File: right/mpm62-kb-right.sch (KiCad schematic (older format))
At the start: 81 parts

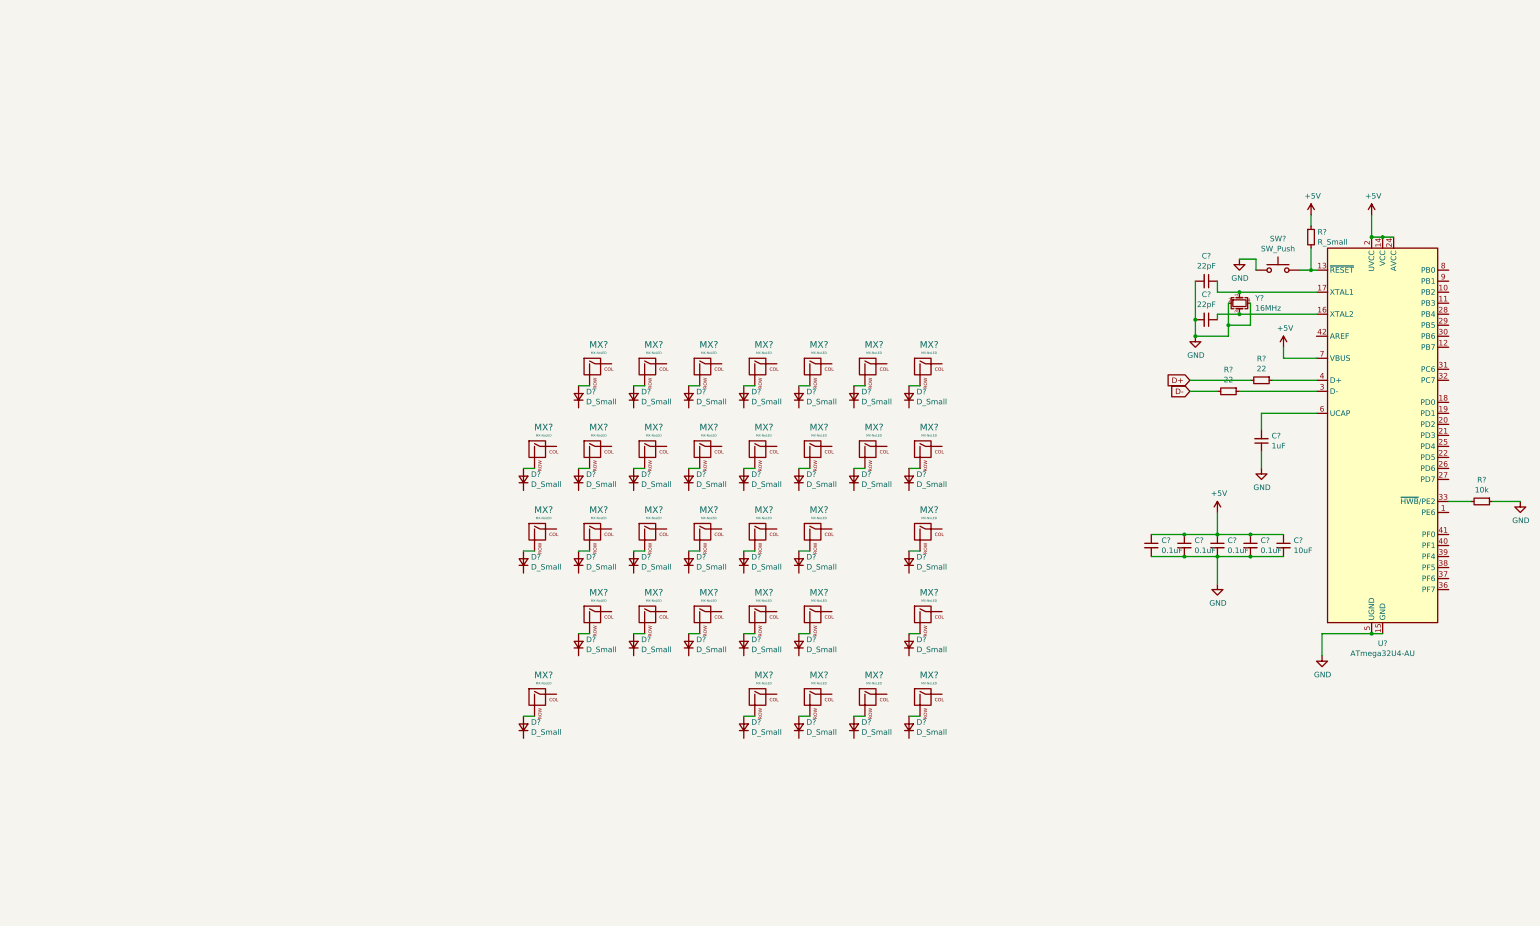
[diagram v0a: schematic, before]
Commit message: complete schematics for both left and right
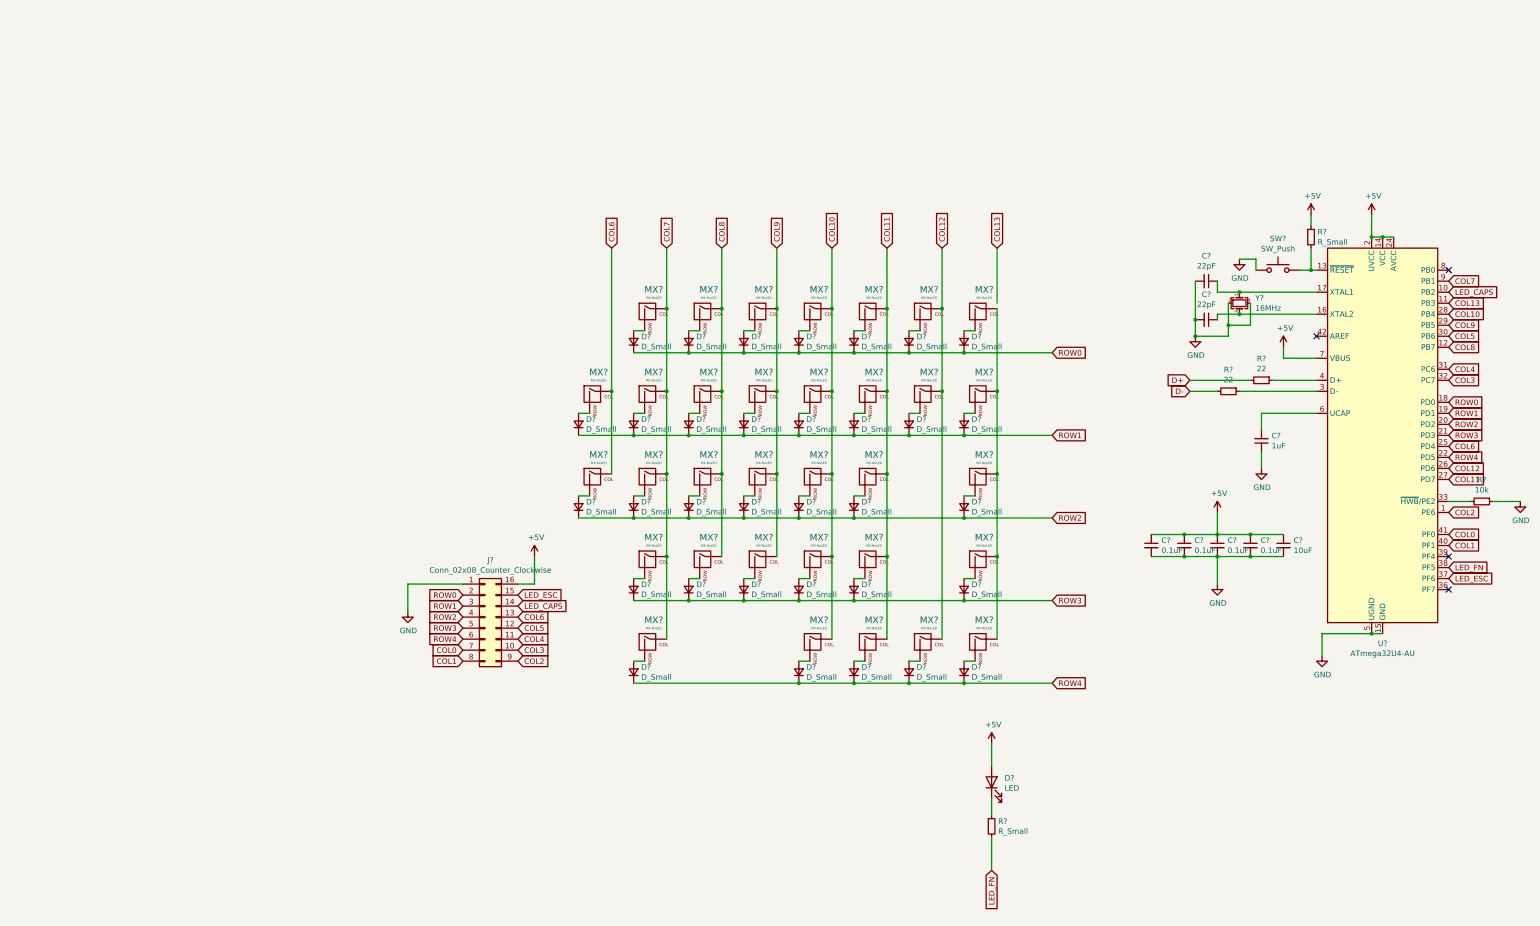
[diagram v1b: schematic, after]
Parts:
- added D?: LED, symbol Device:LED
- added J?: Conn_02x08_Counter_Clockwise, symbol Connector_Generic:Conn_02x08_Counter_Clockwise
- added R?: R_Small, symbol Device:R_Small
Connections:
- net +5V: now also D?.2 (A), J?.16 (Pin_16)
- net GND: now also J?.1 (Pin_1)
- net ROW1: now reaches D?.1 (K)
- net ROW1: now also D?.1 (K), D?.1 (K), D?.1 (K), D?.1 (K), D?.1 (K), D?.1 (K), D?.1 (K), U?.19 (PD1), J?.3 (Pin_3)
- net COL6: now reaches MX?.1 (COL)
- net COL6: now also MX?.1 (COL), U?.25 (PD4), J?.13 (Pin_13)
- net ROW2: now reaches D?.1 (K)
- net ROW2: now also D?.1 (K), D?.1 (K), D?.1 (K), D?.1 (K), D?.1 (K), D?.1 (K), U?.20 (PD2), J?.4 (Pin_4)
- net ROW4: now reaches D?.1 (K)
- net ROW4: now also D?.1 (K), D?.1 (K), D?.1 (K), D?.1 (K), U?.22 (PD5), J?.6 (Pin_6)
- net COL7: now reaches MX?.1 (COL)
- net COL7: now also MX?.1 (COL), MX?.1 (COL), MX?.1 (COL), MX?.1 (COL), U?.9 (PB1)
- net ROW0: now reaches D?.1 (K)
- net ROW0: now also D?.1 (K), D?.1 (K), D?.1 (K), D?.1 (K), D?.1 (K), D?.1 (K), U?.18 (PD0), J?.2 (Pin_2)
- net ROW3: now reaches D?.1 (K)
- net ROW3: now also D?.1 (K), D?.1 (K), D?.1 (K), D?.1 (K), D?.1 (K), U?.21 (PD3), J?.5 (Pin_5)
- net COL8: now reaches MX?.1 (COL)
- net COL8: now also MX?.1 (COL), MX?.1 (COL), MX?.1 (COL), U?.12 (PB7)
- net COL9: now reaches MX?.1 (COL)
- net COL9: now also MX?.1 (COL), MX?.1 (COL), MX?.1 (COL), U?.29 (PB5)
- net COL10: now reaches MX?.1 (COL)
- net COL10: now also MX?.1 (COL), MX?.1 (COL), MX?.1 (COL), MX?.1 (COL), U?.28 (PB4)
- net COL11: now reaches MX?.1 (COL)
- net COL11: now also MX?.1 (COL), MX?.1 (COL), MX?.1 (COL), MX?.1 (COL), U?.27 (PD7)
- net COL12: now reaches MX?.1 (COL)
- net COL12: now also MX?.1 (COL), MX?.1 (COL), U?.26 (PD6)
- net at MX?.1 (COL): now also MX?.1 (COL), MX?.1 (COL), MX?.1 (COL), MX?.1 (COL)
- net COL2: now reaches U?.1 (PE6)
- net COL2: now also J?.9 (Pin_9)
- net LED_CAPS: now reaches U?.10 (PB2)
- net LED_CAPS: now also J?.14 (Pin_14)
- net COL13: now reaches U?.11 (PB3)
- net COL5: now reaches U?.30 (PB6)
- net COL5: now also J?.12 (Pin_12)
- net COL4: now reaches U?.31 (PC6)
- net COL4: now also J?.11 (Pin_11)
- net COL3: now reaches U?.32 (PC7)
- net COL3: now also J?.10 (Pin_10)
- net LED_ESC: now reaches U?.37 (PF6)
- net LED_ESC: now also J?.15 (Pin_15)
- net LED_FN: now reaches U?.38 (PF5)
- net LED_FN: now also R?.2
- net COL1: now reaches U?.40 (PF1)
- net COL1: now also J?.8 (Pin_8)
- net COL0: now reaches U?.41 (PF0)
- net COL0: now also J?.7 (Pin_7)
- new net: D?.1 (K), R?.1
- no-connect marks 0 -> 4
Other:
- moved on the sheet: D?, MX?

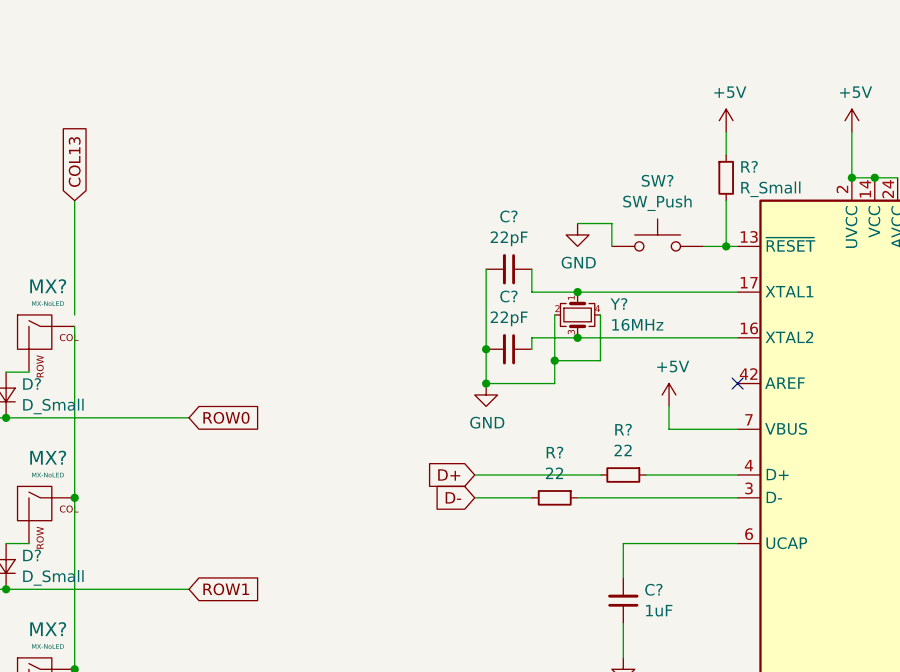
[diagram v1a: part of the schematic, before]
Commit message: Add usb connector. Cleaned up crystal in schematic.
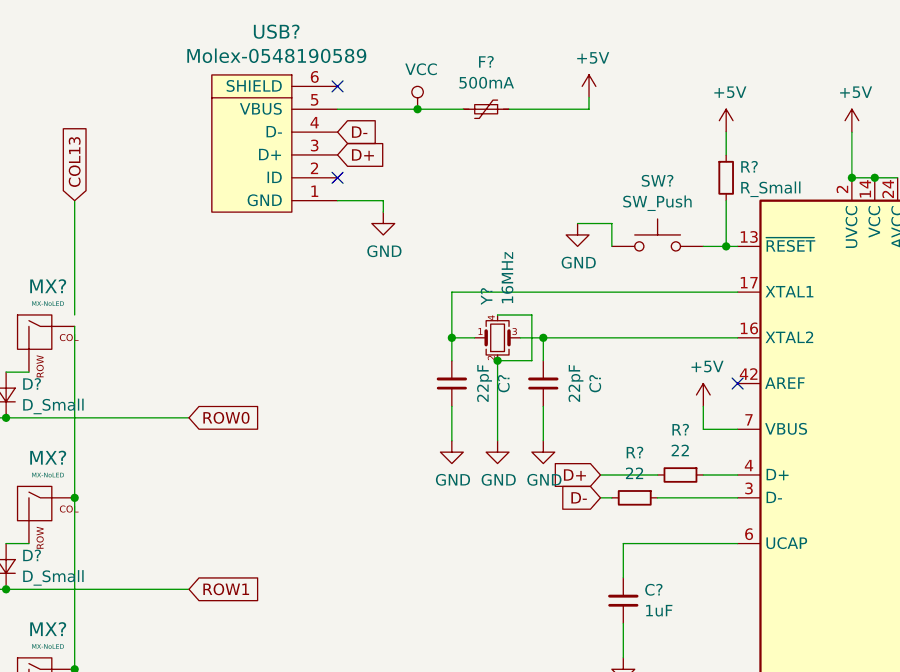
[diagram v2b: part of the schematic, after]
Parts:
- added F?: 500mA, symbol Device:Polyfuse_Small
- added USB?: Molex-0548190589, symbol random-keyboard-parts:Molex-0548190589
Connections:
- net +5V: now also F?.1
- net D+: now also USB?.3 (D+)
- net D-: now also USB?.4 (D-)
- net GND: now also C?.1, C?.1, USB?.1 (GND); no longer C?.2, C?.2
- net at U?.16 (XTAL2), Y?.3: now also C?.2; no longer C?.1
- net at U?.17 (XTAL1), Y?.1: now also C?.2; no longer C?.1
- new net VCC: F?.2, USB?.5 (VBUS)
- no-connect marks 4 -> 6
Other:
- moved on the sheet: C?, R?, Y?
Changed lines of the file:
@@
-$Comp
-L Device:R_Small R?
-U 1 1 5F5B9463
-P 8650 2700
-F 0 "R?" V 8454 2700 50  0000 C CNN
-F 1 "22" V 8545 2700 50  0000 C CNN
-F 2 "" H 8650 2700 50  0001 C CNN
-F 3 "~" H 8650 2700 50  0001 C CNN
-	1    8650 2700
-	0    1    1    0
-$EndComp
 $Comp
 L Device:R_Small R?
 U 1 1 5F5BAB42
-P 8350 2800
-F 0 "R?" V 8154 2800 50  0000 C CNN
-F 1 "22" V 8245 2800 50  0000 C CNN
-F 2 "" H 8350 2800 50  0001 C CNN
-F 3 "~" H 8350 2800 50  0001 C CNN
-	1    8350 2800
+P 8700 2800
+F 0 "R?" V 8504 2800 50  0000 C CNN
+F 1 "22" V 8595 2800 50  0000 C CNN
+F 2 "" H 8700 2800 50  0001 C CNN
+F 3 "~" H 8700 2800 50  0001 C CNN
+	1    8700 2800
 	0    1    1    0
 $EndComp
-Wire Wire Line
-	9150 2700 8750 2700
-Wire Wire Line
-	9150 2800 8450 2800
-Wire Wire Line
-	8250 2800 8000 2800
 $Comp
 L Device:C_Small C?
@@
 L power:+5V #PWR?
 U 1 1 5F5E2F30
-P 8850 2400
-F 0 "#PWR?" H 8850 2250 50  0001 C CNN
-F 1 "+5V" H 8865 2573 50  0000 C CNN
-F 2 "" H 8850 2400 50  0001 C CNN
-F 3 "" H 8850 2400 50  0001 C CNN
-	1    8850 2400
-	1    0    0    -1
-$EndComp
-Wire Wire Line
-	9150 2500 8850 2500
-Wire Wire Line
-	8850 2500 8850 2400
-$Comp
-L power:GND #PWR?
-U 1 1 5F5F4433
-P 8050 2300
-F 0 "#PWR?" H 8050 2050 50  0001 C CNN
-F 1 "GND" H 8055 2127 50  0000 C CNN
-F 2 "" H 8050 2300 50  0001 C CNN
-F 3 "" H 8050 2300 50  0001 C CNN
-	1    8050 2300
-	1    0    0    -1
-$EndComp
-Wire Wire Line
-	8350 2000 8350 2200
-Wire Wire Line
-	8550 2000 8550 2200
-Wire Wire Line
-	8550 2200 8350 2200
-$Comp
-L Device:C_Small C?
-U 1 1 5F600B60
-P 8150 2150
-F 0 "C?" V 7921 2150 50  0000 C CNN
-F 1 "22pF" V 8012 2150 50  0000 C CNN
-F 2 "" H 8150 2150 50  0001 C CNN
-F 3 "~" H 8150 2150 50  0001 C CNN
-	1    8150 2150
-	0    1    1    0
-$EndComp
-$Comp
-L Device:C_Small C?
-U 1 1 5F601B45
-P 8150 1800
-F 0 "C?" V 7921 1800 50  0000 C CNN
-F 1 "22pF" V 8012 1800 50  0000 C CNN
-F 2 "" H 8150 1800 50  0001 C CNN
-F 3 "~" H 8150 1800 50  0001 C CNN
-	1    8150 1800
-	0    1    1    0
-$EndComp
-Wire Wire Line
-	8250 2100 8250 2150
-Wire Wire Line
-	8350 2200 8350 2300
-Wire Wire Line
-	8350 2300 8050 2300
-Connection ~ 8350 2200
-Wire Wire Line
-	8450 2100 8250 2100
-Wire Wire Line
-	9150 2100 8450 2100
-Connection ~ 8450 2100
-$Comp
-L Device:Crystal_GND24_Small Y?
-U 1 1 5F5EE552
-P 8450 2000
-F 0 "Y?" V 8404 2144 50  0000 L CNN
-F 1 "16MHz" V 8495 2144 50  0000 L CNN
-F 2 "" H 8450 2000 50  0001 C CNN
-F 3 "~" H 8450 2000 50  0001 C CNN
-	1    8450 2000
-	0    1    1    0
-$EndComp
-Wire Wire Line
-	8250 1800 8250 1900
-Wire Wire Line
-	8250 1900 8450 1900
-Connection ~ 8450 1900
-Wire Wire Line
-	8450 1900 9150 1900
-Wire Wire Line
-	8050 1800 8050 2150
-Wire Wire Line
-	8050 2150 8050 2300
-Connection ~ 8050 2150
-Connection ~ 8050 2300
+P 9000 2400
+F 0 "#PWR?" H 9000 2250 50  0001 C CNN
+F 1 "+5V" H 9015 2573 50  0000 C CNN
+F 2 "" H 9000 2400 50  0001 C CNN
+F 3 "" H 9000 2400 50  0001 C CNN
+	1    9000 2400
+	1    0    0    -1
+$EndComp
 $Comp
 L Switch:SW_Push SW?
@@
 Wire Wire Line
 	9100 1300 9100 1200
-Wire Wire Line
-	8550 2700 8000 2700
-Text GLabel 8000 2700 0    50   Input ~ 0
+Text GLabel 8550 2700 0    50   Input ~ 0
 D+
-Text GLabel 8000 2800 0    50   Input ~ 0
+Text GLabel 8550 2800 0    50   Input ~ 0
 D-
 Wire Wire Line
@@
 Wire Wire Line
 	6200 6850 6200 7150
+$Comp
+L random-keyboard-parts:Molex-0548190589 USB?
+U 1 1 5F54C701
+P 7100 1300
+F 0 "USB?" V 7637 1267 60  0000 C CNN
+F 1 "Molex-0548190589" V 7531 1267 60  0000 C CNN
+F 2 "" H 7100 1300 60  0001 C CNN
+F 3 "" H 7100 1300 60  0001 C CNN
+	1    7100 1300
+	0    -1   -1   0
+$EndComp
+Text GLabel 7400 1300 2    50   Input ~ 0
+D+
+Text GLabel 7400 1200 2    50   Input ~ 0
+D-
+$Comp
+L power:VCC #PWR?
+U 1 1 5F54F597
+P 7750 1100
+F 0 "#PWR?" H 7750 950 50  0001 C CNN
+F 1 "VCC" H 7767 1273 50  0000 C CNN
+F 2 "" H 7750 1100 50  0001 C CNN
+F 3 "" H 7750 1100 50  0001 C CNN
+	1    7750 1100
+	1    0    0    -1
+$EndComp
+Wire Wire Line
+	7400 1100 7750 1100
+$Comp
+L Device:Polyfuse_Small F?
+U 1 1 5F557989
+P 8050 1100
+F 0 "F?" V 7845 1100 50  0000 C CNN
+F 1 "500mA" V 7936 1100 50  0000 C CNN
+F 2 "" H 8100 900 50  0001 L CNN
+F 3 "~" H 8050 1100 50  0001 C CNN
+	1    8050 1100
+	0    1    1    0
+$EndComp
+Wire Wire Line
+	7750 1100 7950 1100
+Connection ~ 7750 1100
+Wire Wire Line
+	8150 1100 8500 1100
+Wire Wire Line
+	8500 1100 8500 1050
+$Comp
+L power:+5V #PWR?
+U 1 1 5F5674CE
+P 8500 1050
+F 0 "#PWR?" H 8500 900 50  0001 C CNN
+F 1 "+5V" H 8515 1223 50  0000 C CNN
+F 2 "" H 8500 1050 50  0001 C CNN
+F 3 "" H 8500 1050 50  0001 C CNN
+	1    8500 1050
+	1    0    0    -1
+$EndComp
+Wire Wire Line
+	7400 1500 7600 1500
+Wire Wire Line
+	7600 1500 7600 1550
+$Comp
+L power:GND #PWR?
+U 1 1 5F56FA33
+P 7600 1550
+F 0 "#PWR?" H 7600 1300 50  0001 C CNN
+F 1 "GND" H 7605 1377 50  0000 C CNN
+F 2 "" H 7600 1550 50  0001 C CNN
+F 3 "" H 7600 1550 50  0001 C CNN
+	1    7600 1550
+	1    0    0    -1
+$EndComp
+NoConn ~ 7400 1400
+NoConn ~ 7400 1000
+$Comp
+L Device:R_Small R?
+U 1 1 5F5B9463
+P 8900 2700
+F 0 "R?" V 8704 2700 50  0000 C CNN
+F 1 "22" V 8795 2700 50  0000 C CNN
+F 2 "" H 8900 2700 50  0001 C CNN
+F 3 "~" H 8900 2700 50  0001 C CNN
+	1    8900 2700
+	0    1    1    0
+$EndComp
+Wire Wire Line
+	9150 2500 9000 2500
+Wire Wire Line
+	9000 2500 9000 2400
+Wire Wire Line
+	8600 2800 8550 2800
+Wire Wire Line
+	8550 2700 8800 2700
+Wire Wire Line
+	9000 2700 9150 2700
+Wire Wire Line
+	8800 2800 9150 2800
+$Comp
+L Device:Crystal_GND24_Small Y?
+U 1 1 5F5EE552
+P 8100 2100
+F 0 "Y?" V 8054 2244 50  0000 L CNN
+F 1 "16MHz" V 8145 2244 50  0000 L CNN
+F 2 "" H 8100 2100 50  0001 C CNN
+F 3 "~" H 8100 2100 50  0001 C CNN
+	1    8100 2100
+	1    0    0    -1
+$EndComp
+$Comp
+L Device:C_Small C?
+U 1 1 5F601B45
+P 8300 2300
+F 0 "C?" V 8071 2300 50  0000 C CNN
+F 1 "22pF" V 8162 2300 50  0000 C CNN
+F 2 "" H 8300 2300 50  0001 C CNN
+F 3 "~" H 8300 2300 50  0001 C CNN
+	1    8300 2300
+	-1   0    0    1
+$EndComp
+$Comp
+L Device:C_Small C?
+U 1 1 5F600B60
+P 7900 2300
+F 0 "C?" V 7671 2300 50  0000 C CNN
+F 1 "22pF" V 7762 2300 50  0000 C CNN
+F 2 "" H 7900 2300 50  0001 C CNN
+F 3 "~" H 7900 2300 50  0001 C CNN
+	1    7900 2300
+	-1   0    0    1
+$EndComp
+$Comp
+L power:GND #PWR?
+U 1 1 5F5F4433
+P 7900 2550
+F 0 "#PWR?" H 7900 2300 50  0001 C CNN
+F 1 "GND" H 7905 2377 50  0000 C CNN
+F 2 "" H 7900 2550 50  0001 C CNN
+F 3 "" H 7900 2550 50  0001 C CNN
+	1    7900 2550
+	1    0    0    -1
+$EndComp
+Wire Wire Line
+	9150 1900 7900 1900
+Wire Wire Line
+	7900 1900 7900 2100
+Wire Wire Line
+	9150 2100 8300 2100
+Wire Wire Line
+	8300 2200 8300 2100
+Wire Wire Line
+	8300 2100 8200 2100
+Connection ~ 8300 2100
+Wire Wire Line
+	7900 2100 8000 2100
+Wire Wire Line
+	7900 2100 7900 2200
+Connection ~ 7900 2100
+Wire Wire Line
+	8300 2400 8300 2550
+Wire Wire Line
+	7900 2400 7900 2550
+Wire Wire Line
+	8100 2200 8100 2550
+$Comp
+L power:GND #PWR?
+U 1 1 5F6A5C56
+P 8100 2550
+F 0 "#PWR?" H 8100 2300 50  0001 C CNN
+F 1 "GND" H 8105 2377 50  0000 C CNN
+F 2 "" H 8100 2550 50  0001 C CNN
+F 3 "" H 8100 2550 50  0001 C CNN
+	1    8100 2550
+	1    0    0    -1
+$EndComp
+$Comp
+L power:GND #PWR?
+U 1 1 5F6AC356
+P 8300 2550
+F 0 "#PWR?" H 8300 2300 50  0001 C CNN
+F 1 "GND" H 8305 2377 50  0000 C CNN
+F 2 "" H 8300 2550 50  0001 C CNN
+F 3 "" H 8300 2550 50  0001 C CNN
+	1    8300 2550
+	1    0    0    -1
+$EndComp
+Wire Wire Line
+	8100 2000 8250 2000
+Wire Wire Line
+	8250 2000 8250 2200
+Wire Wire Line
+	8250 2200 8100 2200
+Connection ~ 8100 2200
 $EndSCHEMATC
